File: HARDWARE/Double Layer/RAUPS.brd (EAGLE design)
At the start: 67.3 x 62.9 mm, 52 parts, among them Q2 STP55NF06L, Q3 STP55NF06L, U1 ARDUINOR3-BPLACE

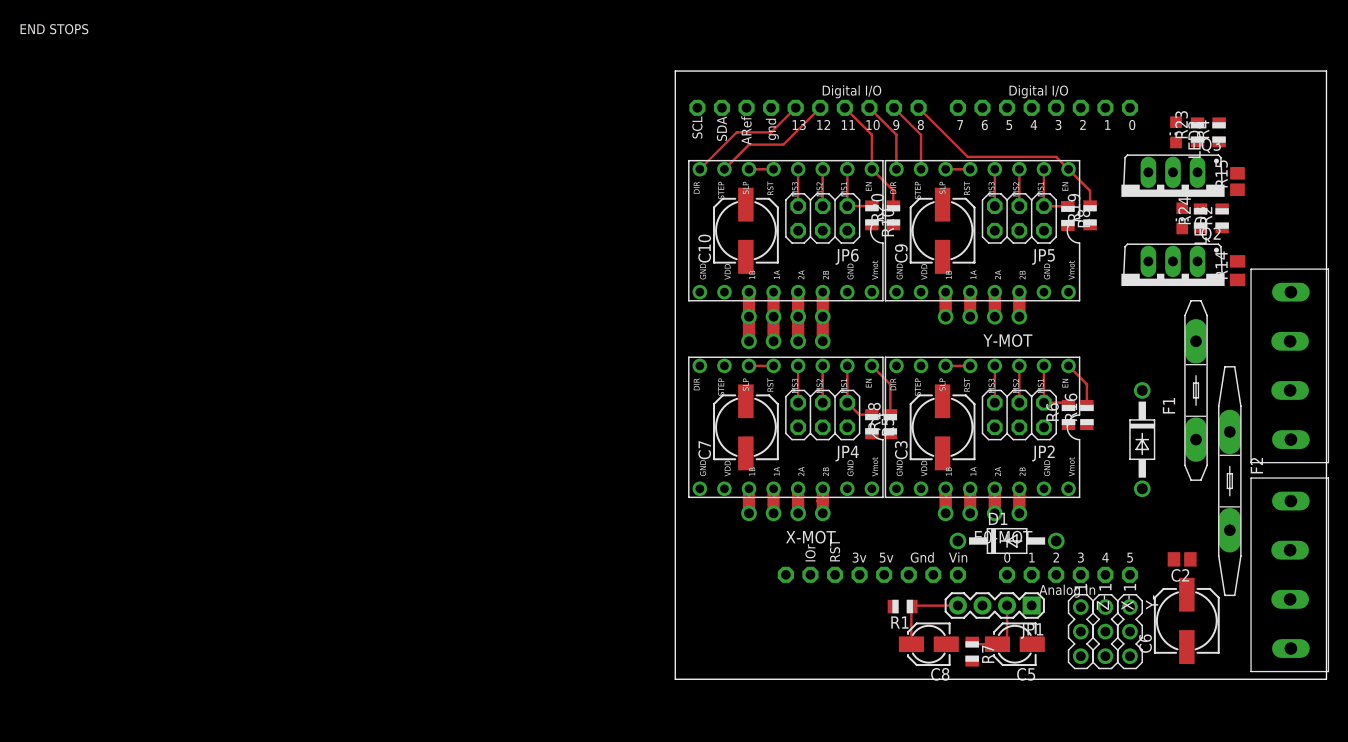
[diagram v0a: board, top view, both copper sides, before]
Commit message: Finished routing of 2 layer board, DRC complete
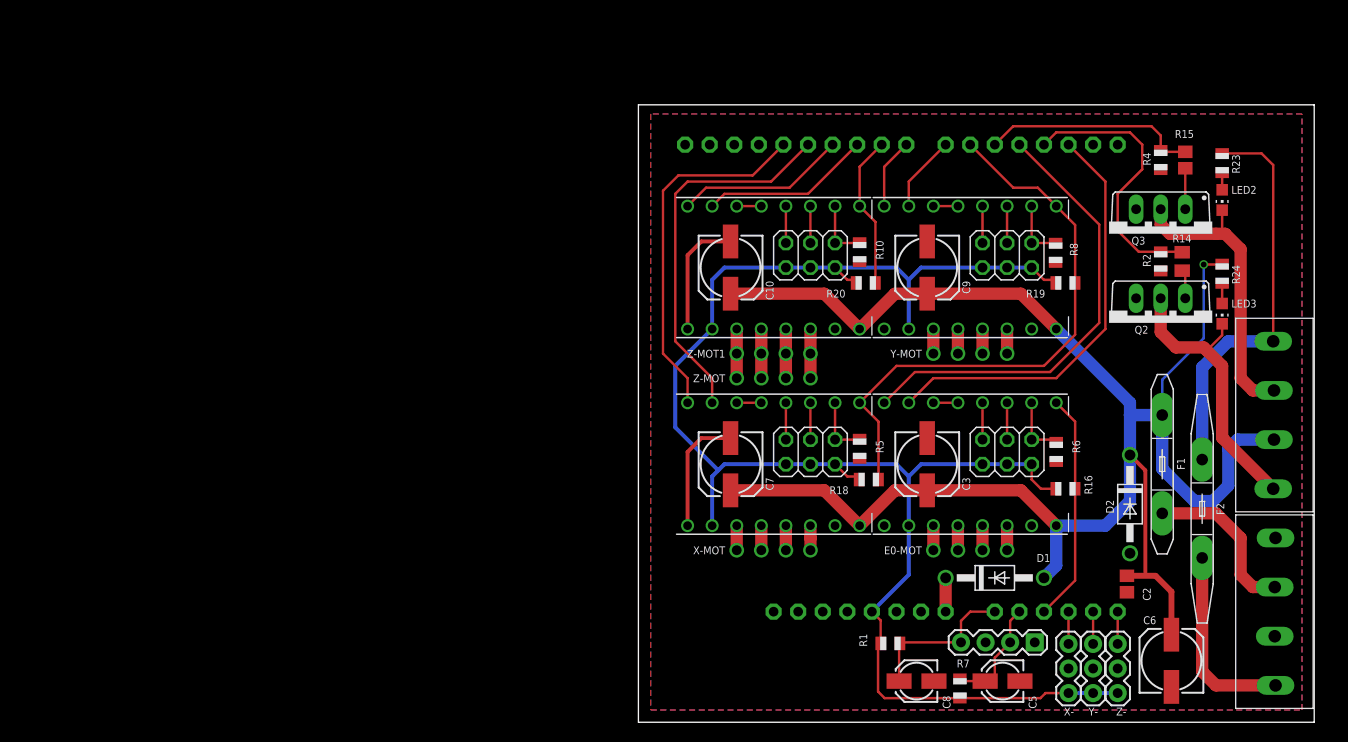
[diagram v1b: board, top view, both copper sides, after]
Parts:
- E0-DRIVE, Y-DRIVE, Z-DRIVE: value A4988BREAKOUT -> POLOLU_A4983CARRIER
- X-, Y-, Z-: device ultimachine:3PIN-HEADER -> SparkFun-Connectors:1X03
- moved U$1 25.4 mm to (65.7, 11.4)
- moved U$2 16.6 mm to (65.7, 31.8), turned to 270 degrees
- moved LED3 10.7 mm to (60.3, 42.2)
- moved LED2 8.45 mm to (60.3, 54.0)
- moved F1 8.38 mm to (54.1, 26.7), turned to 270 degrees
- moved R16 7.94 mm to (44.1, 24.1), turned to 0 degrees
- moved R2 7.75 mm to (54.0, 47.6), turned to 270 degrees
- moved R20 7.55 mm to (23.5, 45.4), turned to 0 degrees
- moved R19 7.43 mm to (44.1, 45.4), turned to 0 degrees
- moved D2 6.79 mm to (50.8, 22.5)
- moved R4 6.68 mm to (54.0, 58.1), turned to 270 degrees
- moved C2 6.25 mm to (50.5, 14.3), turned to 270 degrees
- moved R24 6.13 mm to (60.3, 46.4), turned to 270 degrees
- moved R18 6.13 mm to (23.8, 25.1), turned to 0 degrees
- moved R15 5.84 mm to (56.5, 58.1), turned to 270 degrees
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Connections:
- removed net X-EN: R18.2, X-DRIVE.EN
- net D8: now also U1.D5; no longer U1.D6
- net D9: now also U1.D3; no longer U1.D5
- net E0-DIR: now also U1.D4
- net E0-EN: now also U1.A2
- net E0-STEP: now also U1.D2
- net THERM0: now also U1.A1
- net THERM1: now also U1.A0
- net X-DIR: now also U1.D13
- net X-MIN: now also U1.A3
- net X-STEP: now also U1.D12
- net Y-DIR: now also U1.D8; no longer U1.D10
- net Y-EN: now also R18.2, U1.D6, X-DRIVE.EN; no longer U1.D8
- net Y-MIN: now also U1.A4
- net Y-STEP: now also U1.D7; no longer U1.D9
- net Z-DIR: now also U1.D11; no longer U1.D13
- net Z-EN: now also U1.D9; no longer U1.D11
- net Z-MIN: now also U1.A5
- net Z-STEP: now also U1.D10; no longer U1.D12
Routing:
- net +12V: track 0.00 -> 182.9 mm, vias 0 -> 1
- net VCC: track 0.00 -> 165.6 mm
- net E0-DIR: track 0.00 -> 47.5 mm
- net E0-STEP: track 0.00 -> 44.1 mm
- net +12V2: track 0.00 -> 42.0 mm
- net X-STEP: track 0.00 -> 39.0 mm
- net X-DIR: track 0.00 -> 37.4 mm
- net Y-EN: track 22.8 -> 59.5 mm
- net N$51: track 0.00 -> 31.3 mm
- net N$1: track 0.00 -> 29.6 mm
- net D9: track 0.00 -> 28.7 mm
- net GND: track 0.00 -> 25.3 mm
- net D8: track 0.00 -> 22.5 mm
- net N$53: track 0.00 -> 19.9 mm
- net E0-EN: track 4.87 -> 23.7 mm
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- added copper zone on layer 1, net GND
- added copper zone on layer 16, net GND
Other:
- board size 67.3 x 62.9 mm -> 69.8 x 63.8 mm
- board text removed: "END STOPS"
